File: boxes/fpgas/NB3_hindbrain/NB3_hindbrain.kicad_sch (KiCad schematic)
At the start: 57 parts, among them IC1 FPGA_ICE40UP5K-SG48I, IC2 NOR_Flash_W25Q32JVSSIQ, IC3 FT232HL, J1 MicroUSB_10103594-0001LF, J2 Conn_01x20_Male, J3 Conn_01x20_Male, U1 EEPROM_93LC56BT-I-OT, Y1 Osc_12MHz_ECS-2520MV-120-BN-TR

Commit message: Tweaks to NB3_hindbrain
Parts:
- added IC4: ADC_MCP3004-I-SL, NB3_hindbrain:ADC_MCP3004-I-SL, symbol NB3_hindbrain:ADC_MCP3004-I-SL
- IC3: footprint QFP50P900X900X160-48N -> NB3_hindbrain:USBtoSPI_FT232HL
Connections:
- no-connect marks 24 -> 6
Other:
- note added: "USB to SPI interface (FTDI: FT232HL)"
- note removed: "USB to SPI interface (FTDI: FT4232H)"
- moved on the sheet: C23, C28, IC2, J2, J3, R11, R12, R14, Y1

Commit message: Brainsotmring NB3_hindbrain
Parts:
- removed IC3: FT232HL, NB3_hindbrain:USBtoSPI_FT232HL, symbol NB3_hindbrain:USBtoSPI_FT232HL
- added D10, D11, D12, D13, D14, D15, D16, D17, D18, D19, D20, D21, D22, D23, D24, D25, D26, D27, D28, D29, D30, D31, D32, D33, D34, D35, D4, D5, D6, D7, D8, D9: LED, LED_SMD:LED_0402_1005Metric, symbol Device:LED
- added IC1: FT2232HQ, NB3_hindbrain:USBtoSerial_FT2232HQ, symbol NB3_hindbrain:USBtoSerial_FT2232HQ
- added R14, R16, R17, R18, R19, R20, R21, R22, R23, R24, R25, R26, R27, R28, R29, R30, R31, R32, R33, R34, R35, R36, R37, R38, R39, R40, R41, R42, R43, R44, R45, R46: 150, Resistor_SMD:R_0402_1005Metric, symbol Device:R
- renumbered C28 to C24, C24 to C25, C25 to C26, C26 to C27, C27 to C28, IC1 to IC2, IC2 to IC3, J3 to J2, J2 to J3, R14 to R15
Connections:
- net GND: now also R14.2, R16.2, R17.2, R18.2, R19.2, R20.2, R21.2, R22.2, R23.2, R24.2, R25.2, R26.2, R27.2, R28.2, R29.2, R30.2, R31.2, R32.2, R33.2, R34.2, R35.2, R36.2, R37.2, R38.2, R39.2, R40.2, R41.2, R42.2, R43.2, R44.2, R45.2, R46.2
- new net: D21.1 (K), R32.1
- new net: D30.1 (K), R41.1
- new net: D22.1 (K), R33.1
- new net: D7.1 (K), R18.1
- new net: D17.1 (K), R28.1
- new net: D14.1 (K), R25.1
- new net: D9.1 (K), R20.1
- new net: D10.1 (K), R21.1
- new net: D20.1 (K), R31.1
- new net: D26.1 (K), R37.1
- new net: D25.1 (K), R36.1
- new net: D33.1 (K), R44.1
- new net: D35.1 (K), R46.1
- new net: D8.1 (K), R19.1
- new net: D24.1 (K), R35.1
- new net: D13.1 (K), R24.1
- new net: D15.1 (K), R26.1
- new net: D32.1 (K), R43.1
- new net: D11.1 (K), R22.1
- new net: D23.1 (K), R34.1
- new net: D6.1 (K), R17.1
- new net: D31.1 (K), R42.1
- new net: D27.1 (K), R38.1
- new net: D16.1 (K), R27.1
- new net: D5.1 (K), R16.1
- new net: D18.1 (K), R29.1
- new net: D34.1 (K), R45.1
- new net: D29.1 (K), R40.1
- new net: D28.1 (K), R39.1
- new net: D12.1 (K), R23.1
- new net: D4.1 (K), R14.1
- new net: D19.1 (K), R30.1
- no-connect marks 6 -> 2
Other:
- note added: "16-bit LED debug port?"
- note added: "LEFT"
- note added: "RIGHT"
- note added: "USB to SPI interface (FTDI: FT2232HL)"
- note removed: "USB to SPI interface (FTDI: FT232HL)"
- moved on the sheet: C18, C25, C26, C27, C28, D3, FB1, FB2, IC2, R13, R9

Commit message: Work on NB£_hindbrain schematic
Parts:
- removed C7: 100nF, Capacitor_SMD:C_0402_1005Metric, symbol Device:C
- removed D10, D11, D28, D29, D30, D31, D32, D33, D34, D35, D4, D5, D6, D7, D8, D9: LED, LED_SMD:LED_0402_1005Metric, symbol Device:LED
- removed J2, J3: Conn_01x20_Male, Connector_PinHeader_2.54mm:PinHeader_1x20_P2.54mm_Vertical, symbol Connector:Conn_01x20_Male
- removed R1: 10k, Resistor_SMD:R_0402_1005Metric, symbol Device:R
- removed R14, R16, R17, R18, R19, R20, R21, R22, R39, R40, R41, R42, R43, R44, R45, R46: 150, Resistor_SMD:R_0402_1005Metric, symbol Device:R
- removed R7: 1k, Resistor_SMD:R_0402_1005Metric, symbol Device:R
- added C23: 4.7uF, Capacitor_SMD:C_0603_1608Metric, symbol Device:C
- added C30, C8: 100nF, Capacitor_SMD:C_0402_1005Metric, symbol Device:C
- added D3: LED, LED_SMD:LED_0603_1608Metric, symbol Device:LED
- added J2, J3: Conn_01x20_Pin, Connector_PinHeader_2.54mm:PinHeader_1x20_P2.54mm_Vertical, symbol Connector:Conn_01x20_Pin
- added LED1: CLMVC-FKA-CLBDGL7LBB79353, NB3_hindbrain:RGB_CLMVC-FKA-CLBDGL7LBB79353, symbol NB3_hindbrain:RGB_CLMVC-FKA-CLBDGL7LBB79353
- added R4: 10k, Resistor_SMD:R_0402_1005Metric, symbol Device:R
- added R47, R49, R50, R53: 17k, Resistor_SMD:R_0402_1005Metric, symbol Device:R
- added R48, R51, R52, R54: 33k, Resistor_SMD:R_0402_1005Metric, symbol Device:R
- added R8: 220, Resistor_SMD:R_0402_1005Metric, symbol Device:R
- C18: footprint Capacitor_SMD:C_0603_1608Metric -> Capacitor_SMD:C_0402_1005Metric
- R10: value 150 -> 10k
- R5: value 4.7k -> 12k (1%)
- R6: value 10k -> 1k
- R9: value 12k -> 220
- renumbered C23 to C24, C24 to C25, C25 to C27, C27 to C28, C28 to C29, C8 to C7, D12 to D13, D13 to D14, D14 to D15, D15 to D16, D16 to D17, D17 to D18, D18 to D19, D19 to D20, D20 to D21, D21 to D22, D22 to D23, D23 to D24, D24 to D25, D25 to D26, D26 to D27, D27 to D28, D3 to D4, R4 to R1, R8 to R7
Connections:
- net CRESET_B is gone; now on net CRESET: IC2.8 (CRESET_B)
- net FLASH_SCK is gone; now on net FPGA_SCLK: IC2.15 (IOB_34A_SPI_SCK), IC3.6 (CLK)
- net FLASH_SI is gone; now on net FLASH_MOSI: IC2.14 (IOB_32A_SPI_SO), IC3.5 (DI_(IO0))
- net FLASH_SO is gone; now on net FLASH_MISO: IC2.17 (IOB_33B_SPI_SI), IC3.2 (DO_(IO1))
- net FLASH_SSn is gone; now on net FPGA_CS: IC2.16 (IOB_35B_SPI_SS), IC3.1 (/CS), R12.2
- net +1V8: now also C18.1, IC1.12 (VCORE_1), IC1.37 (VCORE_2), IC1.49 (VREGOUT), IC1.64 (VCORE_3); no longer C18.2
- net +3V3: now also C27.1, D2.2 (A), FB1.2, FB2.2, IC1.20 (VCCIO_1), IC1.31 (VCCIO_2), IC1.42 (VCCIO_3), IC1.50 (VREGIN), IC1.56 (VCCIO_4), IC1.59 (BCBUS7), IC4.13 (VREF), IC4.14 (VDD), R10.1, R6.1, C23.1, C30.1, C8.1, D3.2 (A), J2.20 (Pin_20), J3.20 (Pin_20), LED1.1 (V+), R4.1; no longer C26.1
- net +5V: now also J2.1 (Pin_1), J3.1 (Pin_1); no longer D2.2 (A)
- net CDONE: now also IC1.23 (ADBUS6), J2.16 (Pin_16)
- net CLK_12MHz: now also IC1.2 (OSCI), J2.18 (Pin_18)
- net EECLK: now also IC1.62 (EECLK), R4.2
- net EECS: now also IC1.63 (EECS), R2.2; no longer R1.2
- net FT_VPHY: now also FB1.1, IC1.4 (VPHY); no longer FB2.1
- net FT_VPLL: now also FB2.1, IC1.9 (VPLL); no longer FB1.1
- net GND: now also C18.2, IC1.1 (GND_1), IC1.10 (AGND), IC1.11 (GND_3), IC1.13 (TEST), IC1.15 (GND_4), IC1.25 (GND_5), IC1.35 (GND_6), IC1.47 (GND_7), IC1.5 (GND_2), IC1.51 (GND_8), IC4.12 (AGND), IC4.7 (DGND), R5.1, C23.2, C30.2, C8.2, J2.17 (Pin_17), J2.19 (Pin_19), J2.3 (Pin_3), J2.6 (Pin_6), J3.19 (Pin_19), J3.3 (Pin_3), J3.6 (Pin_6), R48.1, R51.1, R52.1, R54.1; no longer C18.1, R10.2, R6.2, R9.2
- net IOB_0A: now also IC4.9 (DIN)
- net IOB_13B: now also D17.2 (A), J2.11 (Pin_11)
- net IOB_16A: now also D16.2 (A), J2.10 (Pin_10)
- net IOB_18A: now also D15.2 (A), J2.9 (Pin_9)
- net IOB_20A: now also D14.2 (A), J2.8 (Pin_8)
- net IOB_22A: now also D13.2 (A), J2.7 (Pin_7)
- net IOB_2A: now also IC4.10 (DOUT)
- net IOB_4A: now also IC4.11 (CLK)
- net IOB_5B: now also IC4.8 (~{CS}/SHDN)
- net IOB_6A: now also D20.2 (A), J2.14 (Pin_14)
- net IOB_8A: now also D18.2 (A), J2.12 (Pin_12)
- net IOB_9B: now also D19.2 (A), J2.13 (Pin_13)
- net IOT_36B: now also D28.2 (A), J3.7 (Pin_7)
- net IOT_38B: now also D26.2 (A), J3.9 (Pin_9)
- net IOT_39A: now also D27.2 (A), J3.8 (Pin_8)
- net IOT_41A: now also D25.2 (A), J3.10 (Pin_10)
- net IOT_42B: now also D24.2 (A), J3.11 (Pin_11)
- net IOT_43A: now also D23.2 (A), J3.12 (Pin_12)
- net IOT_44B: now also D22.2 (A), J3.13 (Pin_13)
- net IOT_48B: now also D21.2 (A), J3.14 (Pin_14)
- net RGB0: now also LED1.3 (G-)
- net RGB1: now also LED1.2 (B-)
- net RGB2: now also LED1.4 (R-)
- net USB_5V: no longer R5.1
- net USB_DN: now also IC1.7 (DM)
- net USB_DP: now also IC1.8 (DP)
- net at R5.2: now also IC1.6 (REF); no longer R6.1
- net at D2.1 (K): now also R8.1; no longer R10.1
- net at IC1.14 (RESET#): now also R6.2
- net FPGA_SCLK: now reaches IC1.16 (ADBUS0)
- net FPGA_SCLK: now also J3.16 (Pin_16)
- net FLASH_MOSI: now reaches IC1.17 (ADBUS1)
- net FLASH_MOSI: now also J3.15 (Pin_15)
- net FLASH_MISO: now reaches IC1.18 (ADBUS2)
- net FLASH_MISO: now also J3.18 (Pin_18)
- net FPGA_CS: now reaches IC1.21 (ADBUS4)
- net FPGA_CS: now also J3.17 (Pin_17)
- net CRESET: now reaches IC1.24 (ADBUS7)
- net CRESET: now also R10.2, J2.15 (Pin_15)
- net UART_Tx: now reaches IC1.38 (BDBUS0)
- net UART_Tx: now also J2.2 (Pin_2)
- net UART_Rx: now reaches IC1.39 (BDBUS1)
- net UART_Rx: now also J3.2 (Pin_2)
- net Rx_LED: now reaches IC1.54 (BCBUS3)
- net Rx_LED: now also R8.2
- net Tx_LED: now reaches IC1.55 (BCBUS4)
- net Tx_LED: now also R9.2
- net EEDATA: now reaches IC1.61 (EEDATA)
- net EEDATA: now also R3.1, U1.3 (DI)
- net at IC4.1 (CH0): now also R50.1, R51.2
- net at IC4.2 (CH1): now also R47.1, R48.2
- net at IC4.3 (CH2): now also R49.1, R52.2
- net at IC4.4 (CH3): now also R53.1, R54.2
- net at R9.1: now also D3.1 (K)
- net at D4.C, IC2.24 (VPP_2V5): now also C26.1; no longer C27.1
- net EEDATA_I: no longer names the net of R3.2
- net EEDATA_I: now also R1.2, U1.1 (DO); no longer U1.3 (DI)
- removed net EEDATA_O: R2.2, R3.1, U1.1 (DO)
- net FLASH_HOLDn renamed FLASH_HOLD
- net FLASH_WPn renamed FLASH_WP
- net IOB_23B: no longer names the net of IC2.21 (IOB_23B)
- net IOB_24A: no longer names the net of IC2.13 (IOB_24A)
- net IOB_25B_G3: no longer names the net of IC2.20 (IOB_25B_G3)
- net IOB_29B: no longer names the net of IC2.19 (IOB_29B)
- net IOB_31B: no longer names the net of IC2.18 (IOB_31B)
- net IOB_3B_G6: no longer names the net of IC2.44 (IOB_3B_G6)
- net IOT_37A: no longer names the net of IC2.23 (IOT_37A)
- net IOT_45A_G1: no longer names the net of IC2.37 (IOT_45A_G1)
- net IOT_46B_G0: no longer names the net of IC2.35 (IOT_46B_G0)
- net IOT_49A: no longer names the net of IC2.43 (IOT_49A)
- net IOT_50B: no longer names the net of IC2.38 (IOT_50B)
- net IOT_51A: no longer names the net of IC2.42 (IOT_51A)
- new net Analog_0: J3.4 (Pin_4), R50.2
- new net Analog_1: J2.4 (Pin_4), R47.2
- new net Analog_2: J3.5 (Pin_5), R49.2
- new net Analog_3: J2.5 (Pin_5), R53.2
- no-connect marks 2 -> 41
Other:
- note added: "+1.2V"
- note added: "+3.3V"
- note added: "16-bit LED Debug Port"
- note added: "ADC (MCP3004)"
- note added: "Add MOSFETs!"
- note added: "Add PTC (MF-FSMF035X-2)"
- note added: "Noise filter?"
- note added: "Power"
- note added: "Specified in Iceprog"
- note added: "UART"
- note added: "USB to SPI interface (FTDI: FT2232HQ)"
- note added: "Voltage Regulators (LDO)"
- note removed: "16-bit LED debug port?"
- note removed: "USB to SPI interface (FTDI: FT2232HL)"
- note removed: "Voltage Regulators (LDO) +1.2V +3.3V"
- moved on the sheet: C14, C15, C16, C17, C19, C20, C21, C22, C25, C26, C27, C28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

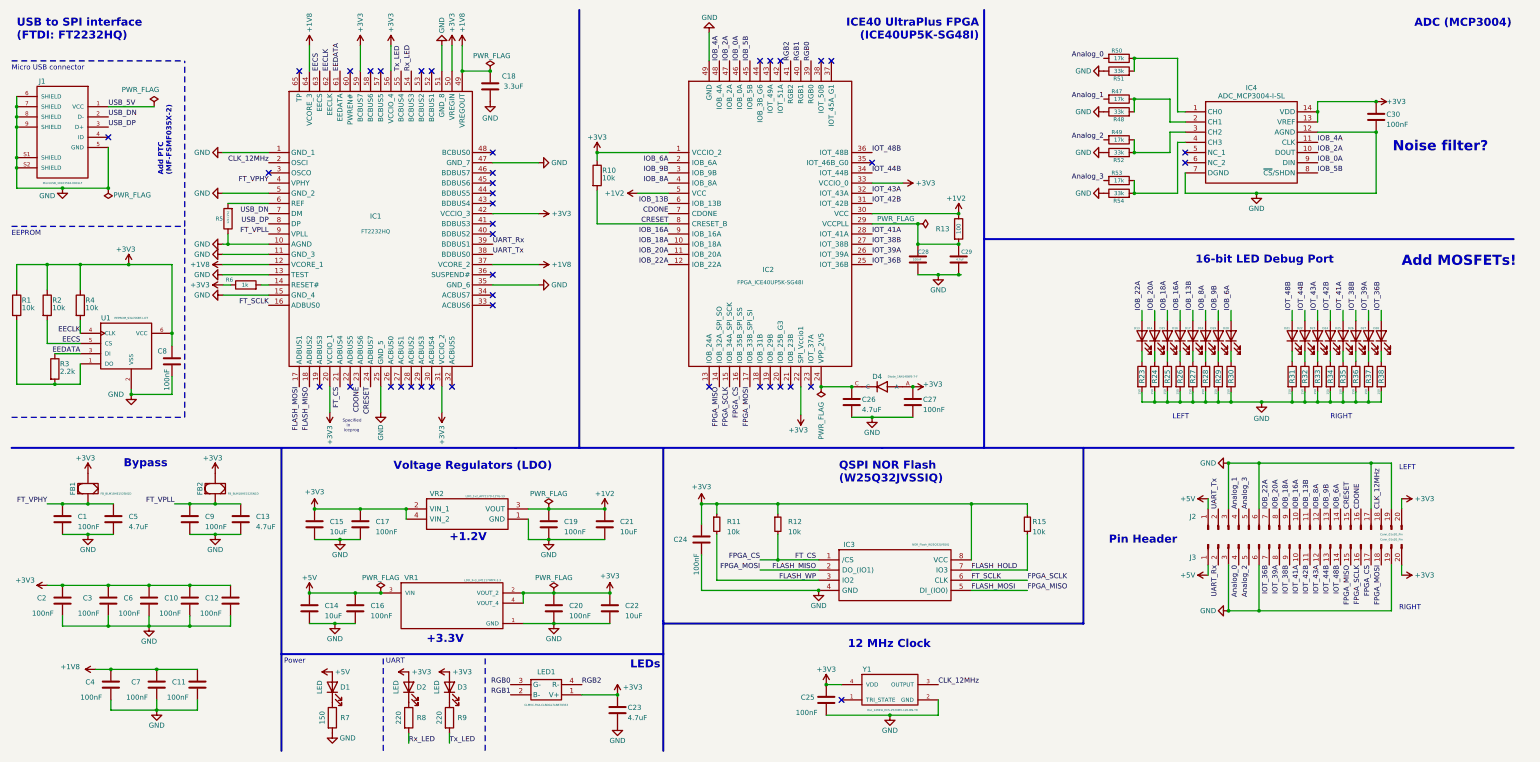
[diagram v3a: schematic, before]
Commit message: NB3_hindbrain updated 1.2V LDO and parts list
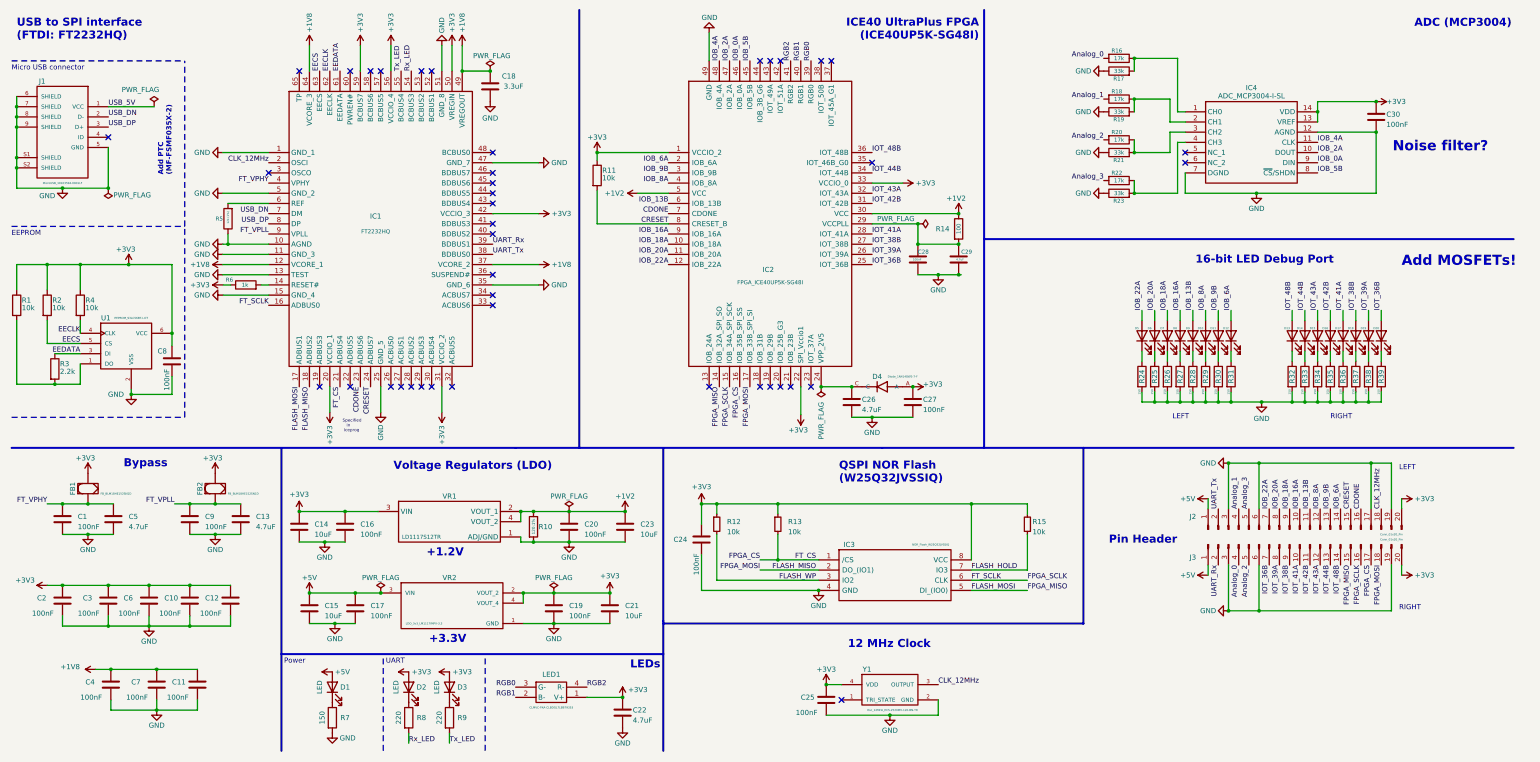
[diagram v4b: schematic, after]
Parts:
- removed VR2: LDO_1v2_AP7217D-12YG-13, NB3_hindbrain:LDO_1v2_AP7217D-12YG-13, symbol NB3_hindbrain:LDO_1v2_AP7217D-12YG-13
- added R10: 120:1%, Resistor_SMD:R_0402_1005Metric, symbol Device:R
- added VR1: LD1117S12TR, NB3_hindbrain:LDO_1v2_LD1117S12TR, symbol NB3_hindbrain:LDO_1v2_LD1117S12TR
- renumbered C15 to C14, C14 to C15, C17 to C16, C16 to C17, C20 to C19, C19 to C20, C22 to C21, C23 to C22, C21 to C23, D18 to D10, D19 to D11, D20 to D12, D21 to D13, D22 to D14, D23 to D15, D24 to D16, D25 to D17, D26 to D18, D27 to D19, D28 to D20, D13 to D5, D14 to D6, D15 to D7, D16 to D8, D17 to D9, R10 to R11, R11 to R12, R12 to R13, R13 to R14, R50 to R16, R51 to R17, R47 to R18, R48 to R19, R49 to R20, R52 to R21, R53 to R22, R54 to R23, R23 to R24, R24 to R25, R25 to R26, R26 to R27, R27 to R28, R28 to R29, R29 to R30, R30 to R31, R31 to R32, R32 to R33, R33 to R34, R34 to R35, R35 to R36, R36 to R37, R37 to R38, R38 to R39, VR1 to VR2
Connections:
- net +1V2: now also R10.1, VR1.2 (VOUT_1), VR1.4 (VOUT_2)
- net +3V3: now also VR1.3 (VIN)
- net GND: now also R10.2, VR1.1 (ADJ/GND)
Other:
- moved on the sheet: C14, C16, C20, C22, C23, LED1

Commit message: Finished NB3 Hindbrain schematic
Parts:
- removed D5: LED, LED_SMD:LED_0402_1005Metric, symbol Device:LED
- removed R24, R25, R26, R27, R28, R29: 150, Resistor_SMD:R_0402_1005Metric, symbol Device:R
- added C30: 10uF, Capacitor_SMD:C_0603_1608Metric, symbol Device:C
- added C31, C33: 100nF, Capacitor_SMD:C_0402_1005Metric, symbol Device:C
- added C32, C35: 10uF, Capacitor_SMD:C_0402_1005Metric, symbol Device:C
- added D21: LED, LED_SMD:LED_0402_1005Metric, symbol Device:LED
- added D4: PRTR5V0U2F,115, NB3_hindbrain:ESD_Diodes_PRTR5V0U2F-115, symbol NB3_hindbrain:ESD_Diodes_PRTR5V0U2F-115
- added F1: MF-FSMF035X-2, NB3_hindbrain:PTC_MF-FSMF035X-2, symbol NB3_hindbrain:PTC_MF-FSMF035X-2
- added G1: LOGO, NB3_hindbrain:Logo_NBB_5mm, symbol NB3_hindbrain:Logo_NBB
- added G2: Logo_VK, NB3_hindbrain:Logo_VK_5mm, symbol NB3_hindbrain:Logo_VK
- added IC5: MCP4812-E_SN, NB3_hindbrain:DAC_MCP4812-E-SN, symbol NB3_hindbrain:DAC_MCP4812-E-SN
- added Q1, Q10, Q11, Q12, Q13, Q14, Q15, Q16, Q2, Q3, Q4, Q5, Q6, Q7, Q8, Q9: RUM001L02T2CL, NB3_hindbrain:MOSFET_Nch_SOT-723_RUM001L02T2CL, symbol NB3_hindbrain:MOSFET_Nch_SOT-723_RUM001L02T2CL
- added R16, R17, R20, R21, R40, R41, R44, R45, R48, R49, R52, R53: 3M3, Resistor_SMD:R_0402_1005Metric, symbol Device:R
- added R18, R19, R42, R43, R46, R47, R50, R51, R54, R55: 680, Resistor_SMD:R_0402_1005Metric, symbol Device:R
- R30, R31, R34, R35, R38, R39: value 150 -> 680
- R32, R33, R36, R37: value 150 -> 3M3
- renumbered C26 to C25, C27 to C26, C28 to C27, C25 to C28, C30 to C34, D4 to D5, R16 to R22, R17 to R23, R18 to R24, R19 to R25, R20 to R26, R21 to R27, R22 to R28, R23 to R29
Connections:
- net +3V3: now also D10.2 (A), D11.2 (A), D12.2 (A), D13.2 (A), D14.2 (A), D15.2 (A), D16.2 (A), D17.2 (A), D18.2 (A), D19.2 (A), D20.2 (A), D6.2 (A), D7.2 (A), D8.2 (A), D9.2 (A), C30.1, C31.1, C32.1, C33.1, C35.1, D21.2 (A), IC5.1 (VDD)
- net +5V: now also F1.2; no longer J2.1 (Pin_1), J3.1 (Pin_1)
- net CDONE: now also J3.6 (Pin_6); no longer J2.16 (Pin_16)
- net CLK_12MHz: now also IC2.35 (IOT_46B_G0), J3.15 (Pin_15); no longer J2.18 (Pin_18)
- net CRESET: now also J3.5 (Pin_5); no longer J2.15 (Pin_15)
- net FLASH_MISO: now also J2.3 (Pin_3); no longer J3.18 (Pin_18)
- net FLASH_MOSI: now also J2.6 (Pin_6); no longer J3.15 (Pin_15)
- net FPGA_CS: now also J2.4 (Pin_4); no longer J3.17 (Pin_17)
- net FPGA_SCLK: now also J2.5 (Pin_5); no longer J3.16 (Pin_16)
- net GND: now also J2.16 (Pin_16), J2.2 (Pin_2), J3.16 (Pin_16), J3.2 (Pin_2), C30.2, C31.2, C32.2, C33.2, C35.2, D4.2 (GND), IC5.7 (VSS), Q1.2 (S), Q10.2 (S), Q11.2 (S), Q12.2 (S), Q13.2 (S), Q14.2 (S), Q15.2 (S), Q16.2 (S), Q2.2 (S), Q3.2 (S), Q4.2 (S), Q5.2 (S), Q6.2 (S), Q7.2 (S), Q8.2 (S), Q9.2 (S), R16.2, R17.2, R20.2, R21.2, R40.2, R41.2, R44.2, R45.2, R48.2, R49.2, R52.2, R53.2; no longer J2.17 (Pin_17), J2.19 (Pin_19), J2.3 (Pin_3), J2.6 (Pin_6), J3.19 (Pin_19), J3.3 (Pin_3), J3.6 (Pin_6), R30.2, R31.2, R34.2, R35.2, R38.2, R39.2
- net IOB_13B: now also Q9.1 (G), R40.1; no longer D9.2 (A)
- net IOB_16A: now also R36.1, Q7.1 (G); no longer D8.2 (A)
- net IOB_18A: now also R32.1, Q5.1 (G); no longer D7.2 (A)
- net IOB_20A: now also Q3.1 (G), R20.1; no longer D6.2 (A)
- net IOB_22A: now also Q1.1 (G), R16.1
- net IOB_6A: now also Q15.1 (G), R52.1; no longer D12.2 (A)
- net IOB_8A: now also Q11.1 (G), R44.1; no longer D10.2 (A)
- net IOB_9B: now also Q13.1 (G), R48.1; no longer D11.2 (A)
- net IOT_36B: now also Q2.1 (G), R17.1; no longer D20.2 (A)
- net IOT_38B: now also R33.1, Q6.1 (G); no longer D18.2 (A)
- net IOT_39A: now also Q4.1 (G), R21.1; no longer D19.2 (A)
- net IOT_41A: now also R37.1, Q8.1 (G); no longer D17.2 (A)
- net IOT_42B: now also Q10.1 (G), R41.1; no longer D16.2 (A)
- net IOT_43A: now also Q12.1 (G), R45.1; no longer D15.2 (A)
- net IOT_44B: now also Q14.1 (G), R49.1; no longer D14.2 (A)
- net IOT_48B: now also Q16.1 (G), R53.1; no longer D13.2 (A)
- net UART_Rx: now also J3.4 (Pin_4); no longer J3.2 (Pin_2)
- net UART_Tx: now also J3.3 (Pin_3); no longer J2.2 (Pin_2)
- net USB_5V: now also J2.1 (Pin_1), J3.1 (Pin_1), D4.5 (V+), F1.1
- net USB_DN: now also D4.3 (i/o_2_1); no longer J1.2 (D-)
- net USB_DP: now also D4.1 (i/o_1_1); no longer J1.3 (D+)
- net at D14.1 (K): now also R42.1; no longer R33.1
- net at R34.1: now also D10.1 (K); no longer D15.1 (K)
- net at D7.1 (K): now also R19.1
- net at D13.1 (K): now also R39.1; no longer R32.1
- net at D19.1 (K): now also R51.1; no longer R38.1
- net at D18.1 (K): now also R50.1; no longer R37.1
- net at D17.1 (K): now also R47.1; no longer R36.1
- net at D6.1 (K): now also R18.1
- net at D8.1 (K): now also R30.1
- net at R35.1: now also D11.1 (K); no longer D16.1 (K)
- net IOB_24A: now reaches IC2.13 (IOB_24A)
- net IOB_24A: now also IC5.2 (~{CS})
- net IOB_31B: now reaches IC2.18 (IOB_31B)
- net IOB_31B: now also IC5.3 (SCK)
- net IOB_29B: now reaches IC2.19 (IOB_29B)
- net IOB_29B: now also IC5.4 (SDI)
- net IOB_23B: now reaches IC2.21 (IOB_23B)
- net IOB_23B: now also IC5.5 (~{LDAC})
- net IOB_3B_G6: now reaches IC2.44 (IOB_3B_G6)
- net IOB_3B_G6: now also J2.15 (Pin_15)
- net at D20.1 (K): now also R54.1; no longer R39.1
- net at D9.1 (K): now also R31.1
- net at D12.1 (K): now also R38.1; no longer R31.1
- net Analog_0 renamed A_in_0
- net A_in_0: now also J2.18 (Pin_18); no longer J3.4 (Pin_4)
- net Analog_1 renamed A_in_1
- net A_in_1: now also J3.18 (Pin_18); no longer J2.4 (Pin_4)
- net Analog_2 renamed A_in_2
- net A_in_2: now also J2.17 (Pin_17); no longer J3.5 (Pin_5)
- net Analog_3 renamed A_in_3
- net A_in_3: now also J3.17 (Pin_17); no longer J2.5 (Pin_5)
- new net: Q2.3 (D), R19.2
- new net: D21.1 (K), R55.1
- new net: Q16.3 (D), R55.2
- new net: Q14.3 (D), R51.2
- new net: Q8.3 (D), R39.2
- new net: Q4.3 (D), R31.2
- new net: D16.1 (K), R46.1
- new net: Q7.3 (D), R38.2
- new net: Q11.3 (D), R46.2
- new net: Q15.3 (D), R54.2
- new net: Q9.3 (D), R42.2
- new net: Q10.3 (D), R43.2
- new net: Q6.3 (D), R35.2
- new net: Q12.3 (D), R47.2
- new net: Q13.3 (D), R50.2
- new net: Q1.3 (D), R18.2
- new net: Q5.3 (D), R34.2
- new net: Q3.3 (D), R30.2
- new net: D15.1 (K), R43.1
- new net A_out_0: IC5.8 (VOUTA), J2.19 (Pin_19)
- new net A_out_1: IC5.6 (VOUTB), J3.19 (Pin_19)
- new net USB_DN_preESD: D4.4 (i/o_2_2), J1.2 (D-)
- new net USB_DP_preESD: D4.6 (i/o_1_2), J1.3 (D+)
- no-connect marks 41 -> 35
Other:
- note added: "2x8 LED Debug Ports"
- note added: "ADC (10-bit, 4 Ch)"
- note added: "DAC (10-bit, 2 Ch)"
- note added: "GBuffer"
- note added: "PTC Fuse"
- note added: "QSPI NOR Flash"
- note added: "USB ESD Protection"
- note removed: "16-bit LED Debug Port"
- note removed: "ADC (MCP3004)"
- note removed: "Add MOSFETs!"
- note removed: "Add PTC (MF-FSMF035X-2)"
- note removed: "Noise filter?"
- note removed: "QSPI NOR Flash (W25Q32JVSSIQ)"
- moved on the sheet: C28, C34, IC4, J2, J3, R22, R23, R24, R25, R26, R27, R28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

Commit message: Work on NB3 Hindbrain routing...
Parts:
- removed R10: 120:1%, Resistor_SMD:R_0402_1005Metric, symbol Device:R
- D2, D3: footprint LED_SMD:LED_0603_1608Metric -> LED_SMD:LED_0402_1005Metric
- R7: value 150 -> 330
- R8, R9: value 220 -> 680
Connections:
- net +5V: no longer D1.2 (A)
- net CDONE: no longer J3.6 (Pin_6)
- net CLK_12MHz: now also J2.3 (Pin_3); no longer J3.15 (Pin_15)
- net CRESET: now also J2.4 (Pin_4); no longer J3.5 (Pin_5)
- net FLASH_MISO: now also J3.5 (Pin_5); no longer J2.3 (Pin_3)
- net FLASH_MOSI: now also J3.4 (Pin_4); no longer J2.6 (Pin_6)
- net FPGA_CS: now also J3.6 (Pin_6); no longer J2.4 (Pin_4)
- net FPGA_SCLK: now also J3.3 (Pin_3); no longer J2.5 (Pin_5)
- net UART_Rx: now also J2.6 (Pin_6); no longer J3.4 (Pin_4)
- net UART_Tx: now also J2.5 (Pin_5); no longer J3.3 (Pin_3)
- net USB_5V: now also D1.2 (A)
- net IOB_25B_G3: now reaches IC2.20 (IOB_25B_G3)
- net IOB_25B_G3: now also J3.15 (Pin_15)
- no-connect marks 35 -> 34

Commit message: Hmm....wiring chaos (NB3 Hindbrain)
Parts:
- removed C35: 10uF, Capacitor_SMD:C_0402_1005Metric, symbol Device:C
- added C36, C39: 10uF, Capacitor_SMD:C_0603_1608Metric, symbol Device:C
- added C37, C38: 100nF, Capacitor_SMD:C_0402_1005Metric, symbol Device:C
- C18: value 3.3uF -> 4.7uF; footprint Capacitor_SMD:C_0402_1005Metric -> Capacitor_SMD:C_0603_1608Metric
- C32: footprint Capacitor_SMD:C_0402_1005Metric -> Capacitor_SMD:C_0603_1608Metric
- D1: footprint LED_SMD:LED_0603_1608Metric -> LED_SMD:LED_0402_1005Metric
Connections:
- net +1V2: now also C36.1, C37.2, C38.2, C39.1
- net GND: now also C36.2, C37.1, C38.1, C39.2
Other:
- moved on the sheet: C1, C10, C11, C12, C13, C2, C3, C4, C5, C6, C7, C9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
